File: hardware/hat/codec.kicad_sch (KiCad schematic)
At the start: 62 parts, among them J3 LineIn, J4 LineOut, J5 Headphone, U4 MAX98089ETN_T, Y1 12.288MHz

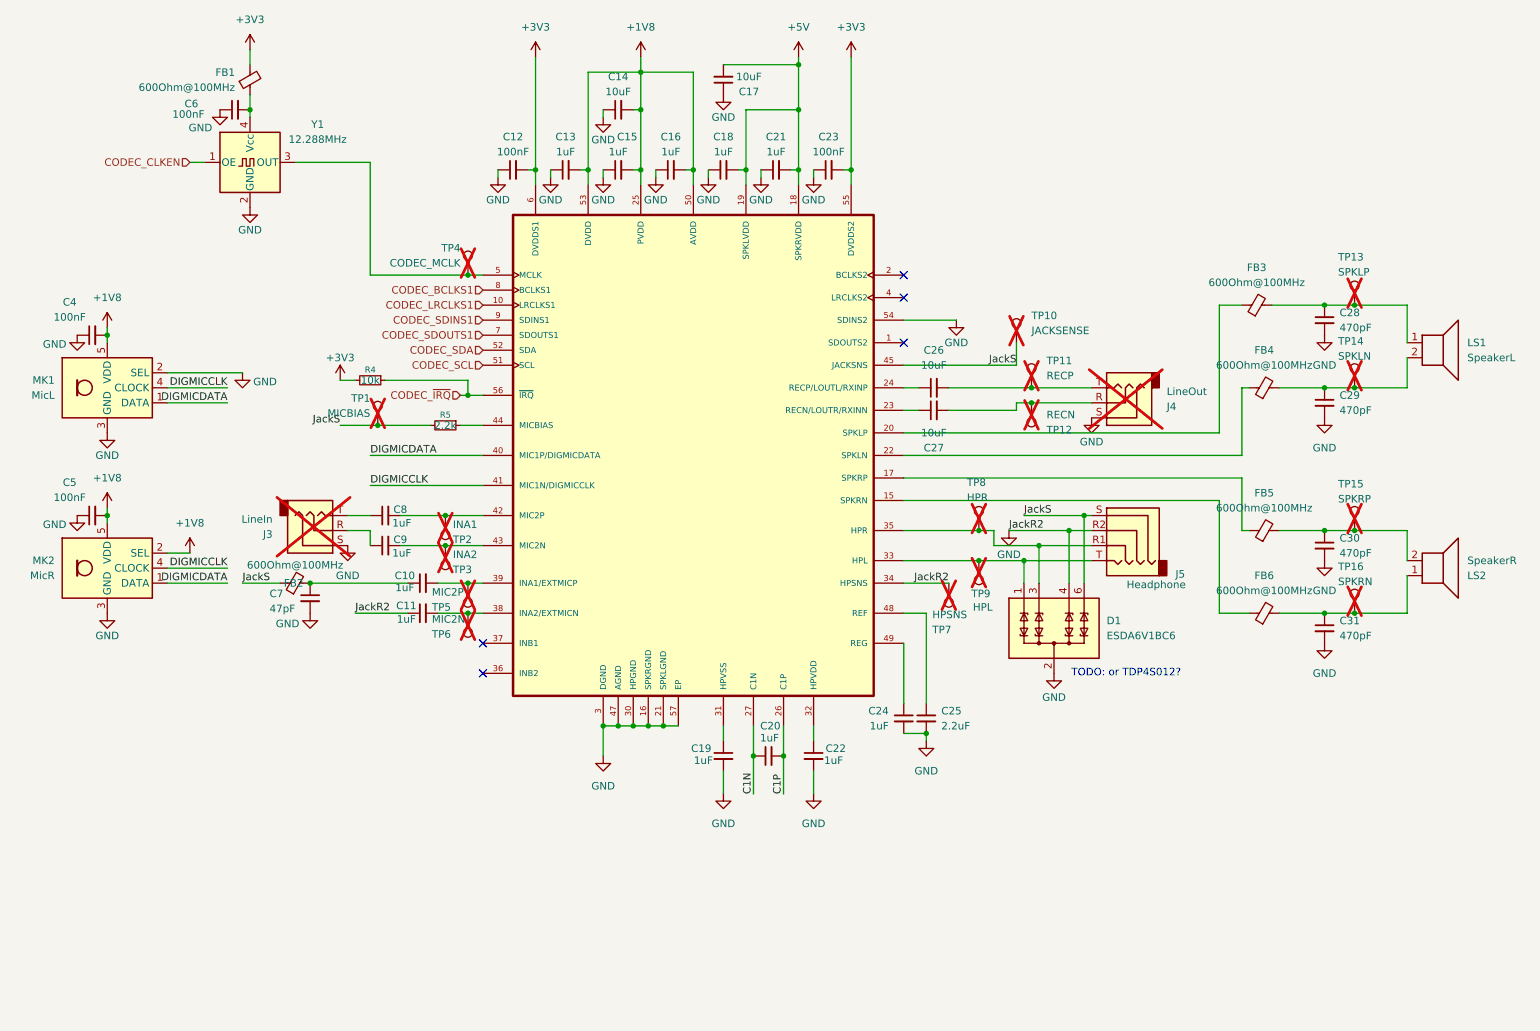
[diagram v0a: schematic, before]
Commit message: make hat 100 x sheetnum
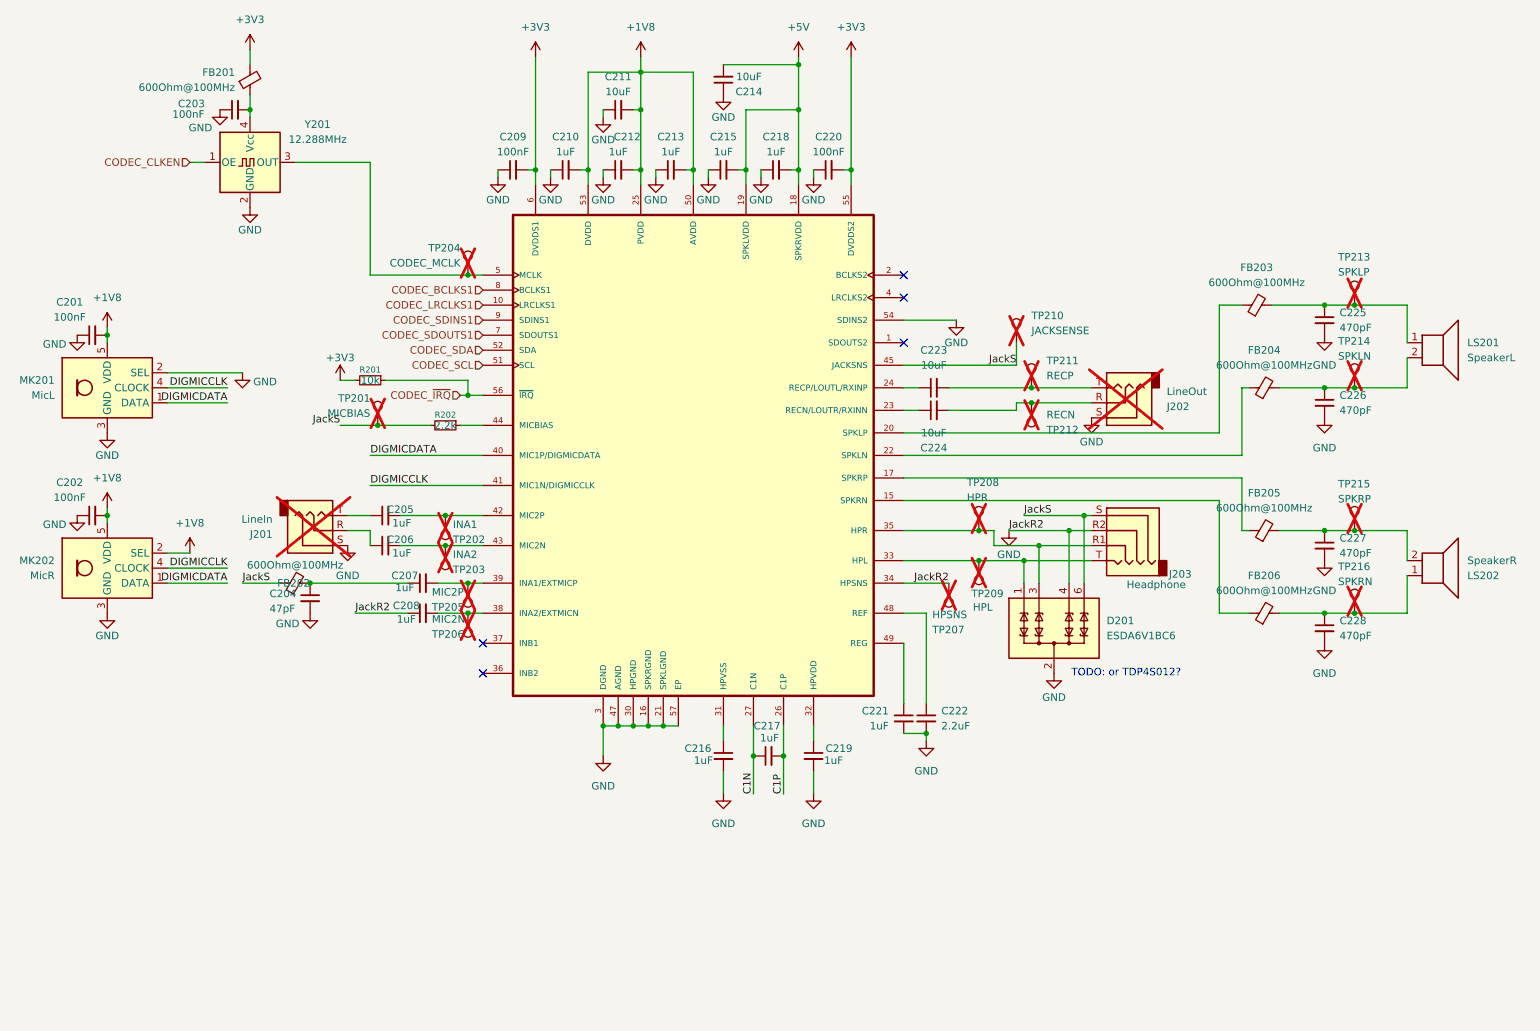
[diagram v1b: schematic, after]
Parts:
- renumbered C4 to C201, C5 to C202, C6 to C203, C7 to C204, C8 to C205, C9 to C206, C10 to C207, C11 to C208, C12 to C209, C13 to C210, C14 to C211, C15 to C212, C16 to C213, C17 to C214, C18 to C215, C19 to C216, C20 to C217, C21 to C218, C22 to C219, C23 to C220, C24 to C221, C25 to C222, C26 to C223, C27 to C224, C28 to C225, C29 to C226, C30 to C227, C31 to C228, D1 to D201, FB1 to FB201, FB2 to FB202, FB3 to FB203, FB4 to FB204, FB5 to FB205, FB6 to FB206, J3 to J201, J4 to J202, J5 to J203, LS1 to LS201, LS2 to LS202, MK1 to MK201, MK2 to MK202, R4 to R201, R5 to R202, TP1 to TP201, TP2 to TP202, TP3 to TP203, TP4 to TP204, TP5 to TP205, TP6 to TP206, TP7 to TP207, TP8 to TP208, TP9 to TP209, TP10 to TP210, TP11 to TP211, TP12 to TP212, TP13 to TP213, TP14 to TP214, TP15 to TP215, TP16 to TP216, U4 to U201, Y1 to Y201

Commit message: move ldo into audio sheet
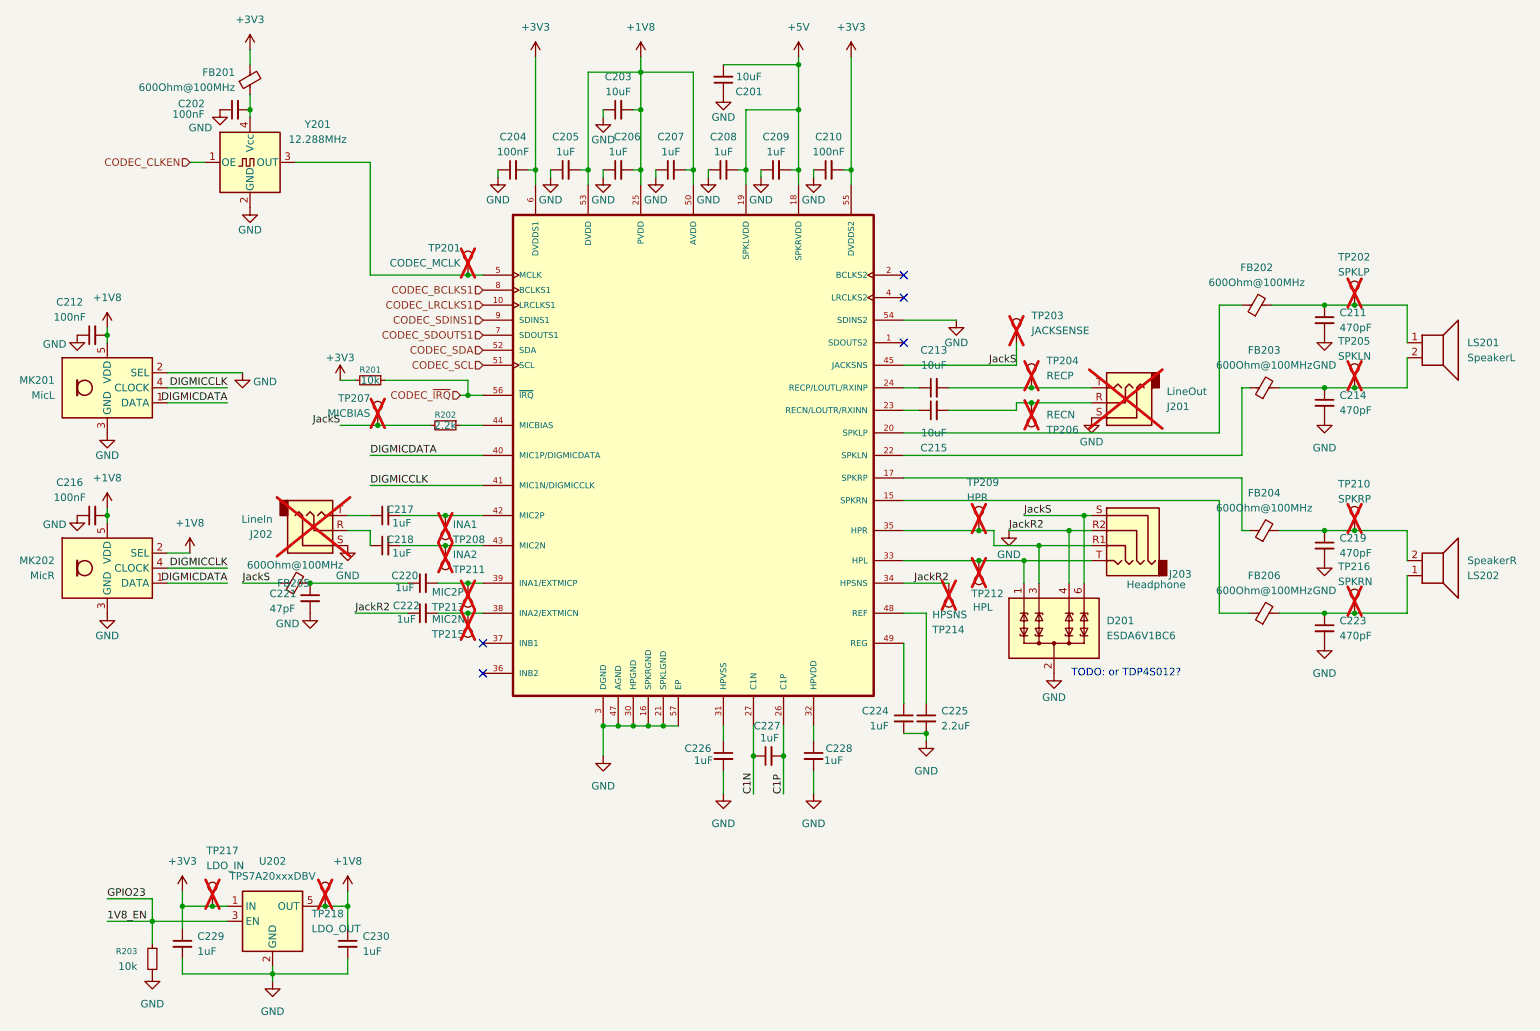
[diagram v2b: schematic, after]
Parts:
- added C229, C230: 1uF, Capacitor_SMD:C_0805_2012Metric, symbol Device:C_Small
- added R203: 10k, Resistor_SMD:R_0805_2012Metric, symbol Device:R_Small
- added TP217: LDO_IN, TestPoint:TestPoint_Pad_D2.0mm, symbol Connector:TestPoint
- added TP218: LDO_OUT, TestPoint:TestPoint_Pad_D2.0mm, symbol Connector:TestPoint
- added U202: TPS7A20xxxDBV, Package_TO_SOT_SMD:SOT-23-5, symbol Regulator_Linear:TPS7A20xxxDBV
- renumbered C214 to C201, C203 to C202, C211 to C203, C209 to C204, C210 to C205, C212 to C206, C213 to C207, C215 to C208, C218 to C209, C220 to C210, C225 to C211, C201 to C212, C223 to C213, C226 to C214, C224 to C215, C202 to C216, C205 to C217, C206 to C218, C227 to C219, C207 to C220, C204 to C221, C208 to C222, C228 to C223, C221 to C224, C222 to C225, C216 to C226, C217 to C227, C219 to C228, FB203 to FB202, FB204 to FB203, FB205 to FB204, FB202 to FB205, J202 to J201, J201 to J202, TP204 to TP201, TP213 to TP202, TP210 to TP203, TP211 to TP204, TP214 to TP205, TP212 to TP206, TP201 to TP207, TP202 to TP208, TP208 to TP209, TP215 to TP210, TP203 to TP211, TP209 to TP212, TP205 to TP213, TP207 to TP214, TP206 to TP215
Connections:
- net +1V8: now also C230.1, TP218.1, U202.5 (OUT)
- net +3V3: now also C229.1, TP217.1, U202.1 (IN)
- net GND: now also C229.2, C230.2, R203.2, U202.2 (GND)
- new net 1V8_EN: R203.1, U202.3 (EN)
